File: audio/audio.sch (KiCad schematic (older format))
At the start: 62 parts, among them J1 Conn_01x02, J2 Conn_01x03, J3 Conn_01x05, U1 LM324DT, U2 LM324DT

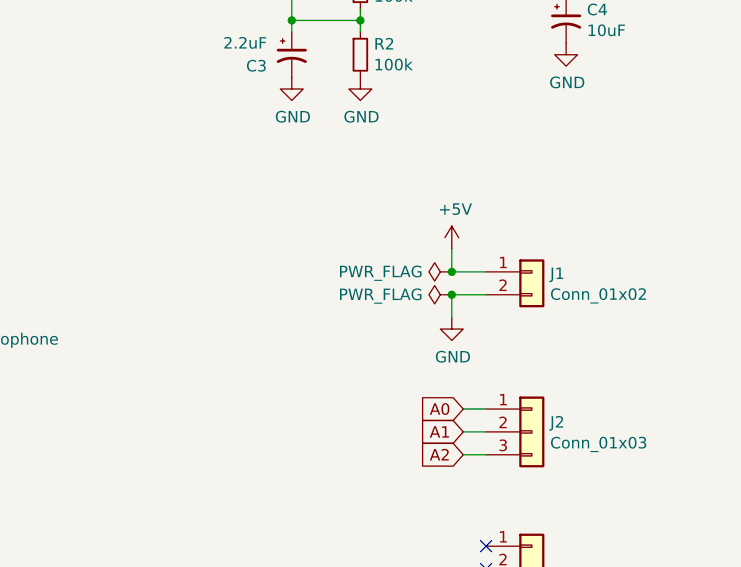
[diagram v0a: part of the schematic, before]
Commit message: properly orient pcb
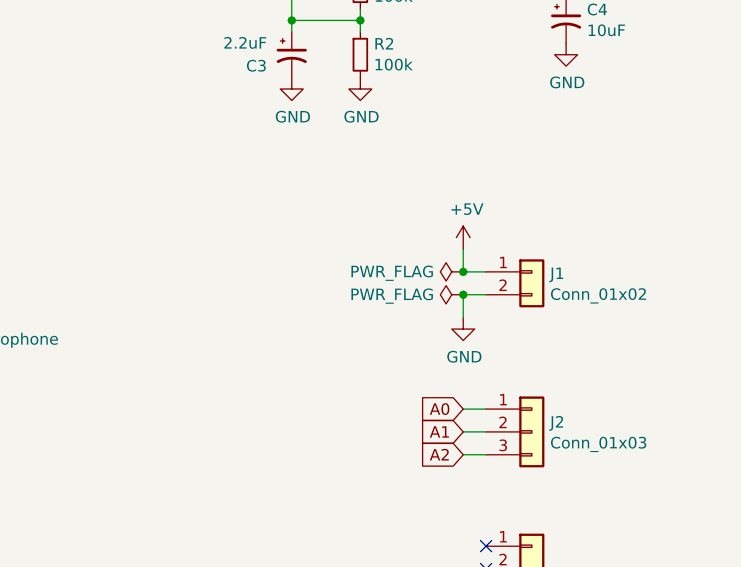
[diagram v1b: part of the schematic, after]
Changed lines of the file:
@@
 $EndComp
 Wire Wire Line
-	8500 4300 8350 4300
+	8400 4300 8400 4200
 Wire Wire Line
-	8350 4300 8350 4200
-Wire Wire Line
-	8500 4400 8350 4400
-Wire Wire Line
-	8350 4400 8350 4500
+	8400 4400 8400 4500
 $Comp
 L power:+5V #PWR013
 U 1 1 6095305C
-P 8350 4200
-F 0 "#PWR013" H 8350 4050 50  0001 C CNN
-F 1 "+5V" H 8365 4373 50  0000 C CNN
-F 2 "" H 8350 4200 50  0001 C CNN
-F 3 "" H 8350 4200 50  0001 C CNN
-	1    8350 4200
+P 8400 4200
+F 0 "#PWR013" H 8400 4050 50  0001 C CNN
+F 1 "+5V" H 8415 4373 50  0000 C CNN
+F 2 "" H 8400 4200 50  0001 C CNN
+F 3 "" H 8400 4200 50  0001 C CNN
+	1    8400 4200
 	1    0    0    -1
 $EndComp
@@
 L power:PWR_FLAG #FLG01
 U 1 1 609539E9
-P 8350 4300
-F 0 "#FLG01" H 8350 4375 50  0001 C CNN
-F 1 "PWR_FLAG" V 8350 4427 50  0000 L CNN
-F 2 "" H 8350 4300 50  0001 C CNN
-F 3 "~" H 8350 4300 50  0001 C CNN
-	1    8350 4300
+P 8400 4300
+F 0 "#FLG01" H 8400 4375 50  0001 C CNN
+F 1 "PWR_FLAG" V 8400 4427 50  0000 L CNN
+F 2 "" H 8400 4300 50  0001 C CNN
+F 3 "~" H 8400 4300 50  0001 C CNN
+	1    8400 4300
 	0    -1   -1   0
 $EndComp
-Connection ~ 8350 4300
+Connection ~ 8400 4300
 $Comp
 L power:PWR_FLAG #FLG02
 U 1 1 60954308
-P 8350 4400
-F 0 "#FLG02" H 8350 4475 50  0001 C CNN
-F 1 "PWR_FLAG" V 8350 4527 50  0000 L CNN
-F 2 "" H 8350 4400 50  0001 C CNN
-F 3 "~" H 8350 4400 50  0001 C CNN
-	1    8350 4400
+P 8400 4400
+F 0 "#FLG02" H 8400 4475 50  0001 C CNN
+F 1 "PWR_FLAG" V 8400 4527 50  0000 L CNN
+F 2 "" H 8400 4400 50  0001 C CNN
+F 3 "~" H 8400 4400 50  0001 C CNN
+	1    8400 4400
 	0    -1   -1   0
 $EndComp
-Connection ~ 8350 4400
+Connection ~ 8400 4400
 $Comp
 L power:GND #PWR014
 U 1 1 60954CB4
-P 8350 4500
-F 0 "#PWR014" H 8350 4250 50  0001 C CNN
-F 1 "GND" H 8355 4327 50  0000 C CNN
-F 2 "" H 8350 4500 50  0001 C CNN
-F 3 "" H 8350 4500 50  0001 C CNN
-	1    8350 4500
+P 8400 4500
+F 0 "#PWR014" H 8400 4250 50  0001 C CNN
+F 1 "GND" H 8405 4327 50  0000 C CNN
+F 2 "" H 8400 4500 50  0001 C CNN
+F 3 "" H 8400 4500 50  0001 C CNN
+	1    8400 4500
 	1    0    0    -1
 $EndComp
@@
 	-1   0    0    1
 $EndComp
+Wire Wire Line
+	8500 4300 8400 4300
+Wire Wire Line
+	8500 4400 8400 4400
 $EndSCHEMATC

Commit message: errata 2: fix footprints
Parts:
- J1: footprint Connector_PinSocket_2.54mm:PinSocket_1x02_P2.54mm_Vertical -> df-parts:310-XX-102-41-001000
- J2: footprint Connector_PinSocket_2.54mm:PinSocket_1x03_P2.54mm_Vertical -> df-parts:310-XX-103-41-001000
- J3: footprint Connector_PinSocket_2.54mm:PinSocket_1x05_P2.54mm_Vertical -> df-parts:310-XX-105-41-001000
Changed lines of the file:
@@
 F 0 "J1" H 8780 4292 50  0000 L CNN
 F 1 "Conn_01x02" H 8780 4201 50  0000 L CNN
-F 2 "Connector_PinSocket_2.54mm:PinSocket_1x02_P2.54mm_Vertical" H 8700 4300 50  0001 C CNN
+F 2 "df-parts:310-XX-102-41-001000" H 8700 4300 50  0001 C CNN
 F 3 "~" H 8700 4300 50  0001 C CNN
 	1    8700 4300
@@
 F 0 "J2" H 8780 5042 50  0000 L CNN
 F 1 "Conn_01x03" H 8780 4951 50  0000 L CNN
-F 2 "Connector_PinSocket_2.54mm:PinSocket_1x03_P2.54mm_Vertical" H 8700 5000 50  0001 C CNN
+F 2 "df-parts:310-XX-103-41-001000" H 8700 5000 50  0001 C CNN
 F 3 "~" H 8700 5000 50  0001 C CNN
 	1    8700 5000
@@
 F 0 "J3" H 8780 5742 50  0000 L CNN
 F 1 "Conn_01x05" H 8780 5651 50  0000 L CNN
-F 2 "Connector_PinSocket_2.54mm:PinSocket_1x05_P2.54mm_Vertical" H 8700 5700 50  0001 C CNN
+F 2 "df-parts:310-XX-105-41-001000" H 8700 5700 50  0001 C CNN
 F 3 "~" H 8700 5700 50  0001 C CNN
 	1    8700 5700
